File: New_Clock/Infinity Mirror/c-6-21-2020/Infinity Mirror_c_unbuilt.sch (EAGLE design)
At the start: 19 parts, among them IC1 MSGEQ7P, J1 Vsupply, J2 AUDIO_POTS, J3 LED, U1 DS1307, Y1 32.768kHz

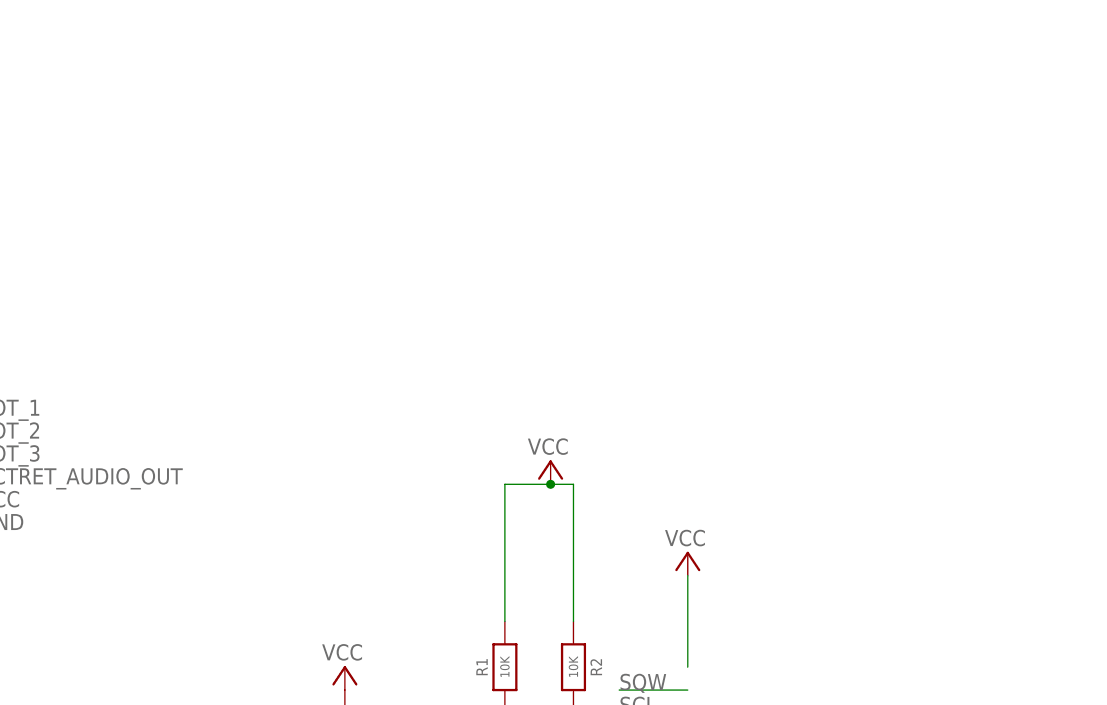
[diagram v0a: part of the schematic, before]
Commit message: created rec v with a larger board with integrated 8 throw switches. found 3D models and ported circuit box for editing in Fusion. NOTE: THIS CAD IS NOT EXACTLY THE SAME AS THE REAL CLOCK
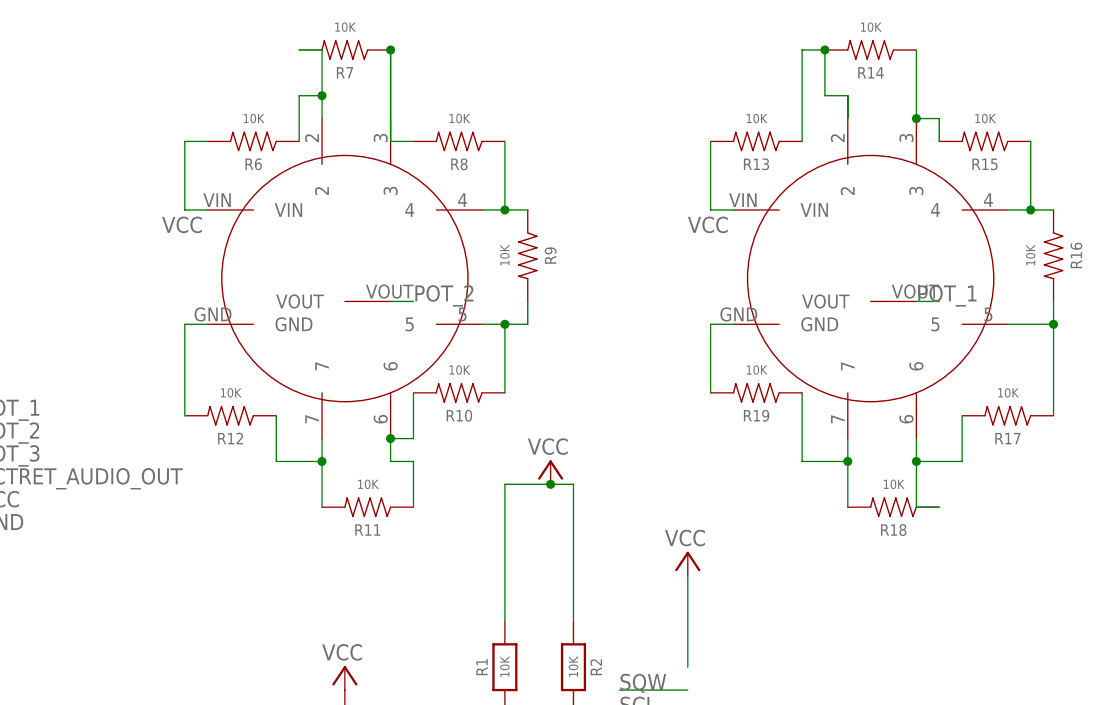
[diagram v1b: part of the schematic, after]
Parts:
- added R10, R11, R12, R13, R14, R15, R16, R17, R18, R19, R6, R7, R8, R9: 10K, RC1a_Main_2-20-2018_m:SPARKFUN-PASSIVES_RESISTOR0805-RES
- added U$2, U$3: ROTARY-SWITCH-8POS, _111_IH:ROTARY-SWITCH-8POS
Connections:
- new net N$1: R8.1, R9.1, U$2.4
- new net N$12: R16.2, R17.1, U$3.5
- new net N$13: R17.2, R18.1, U$3.6
- new net N$14: R18.2, R19.1, U$3.7
- new net N$15: R19.2, U$3.GND
- new net N$17: R13.1, R14.2, U$3.2
- new net N$18: R14.1, R15.2, U$3.3
- new net N$19: R15.1, R16.1, U$3.4
- new net N$2: R7.1, R8.2, U$2.3
- new net N$3: R6.1, R7.2, U$2.2
- new net N$5: R12.2, U$2.GND
- new net N$6: R11.2, R12.1, U$2.7
- new net N$7: R10.2, R11.1, U$2.6
- new net N$9: R10.1, R9.2, U$2.5
- net POT_1: now also U$3.VOUT
- net POT_2: now also U$2.VOUT
- net VCC: now also R13.2, R6.2, U$2.VIN, U$3.VIN
